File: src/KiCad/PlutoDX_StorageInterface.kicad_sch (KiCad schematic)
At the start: 14 parts, among them J2 Micro_SD_Card_Det_Hirose_DM3AT

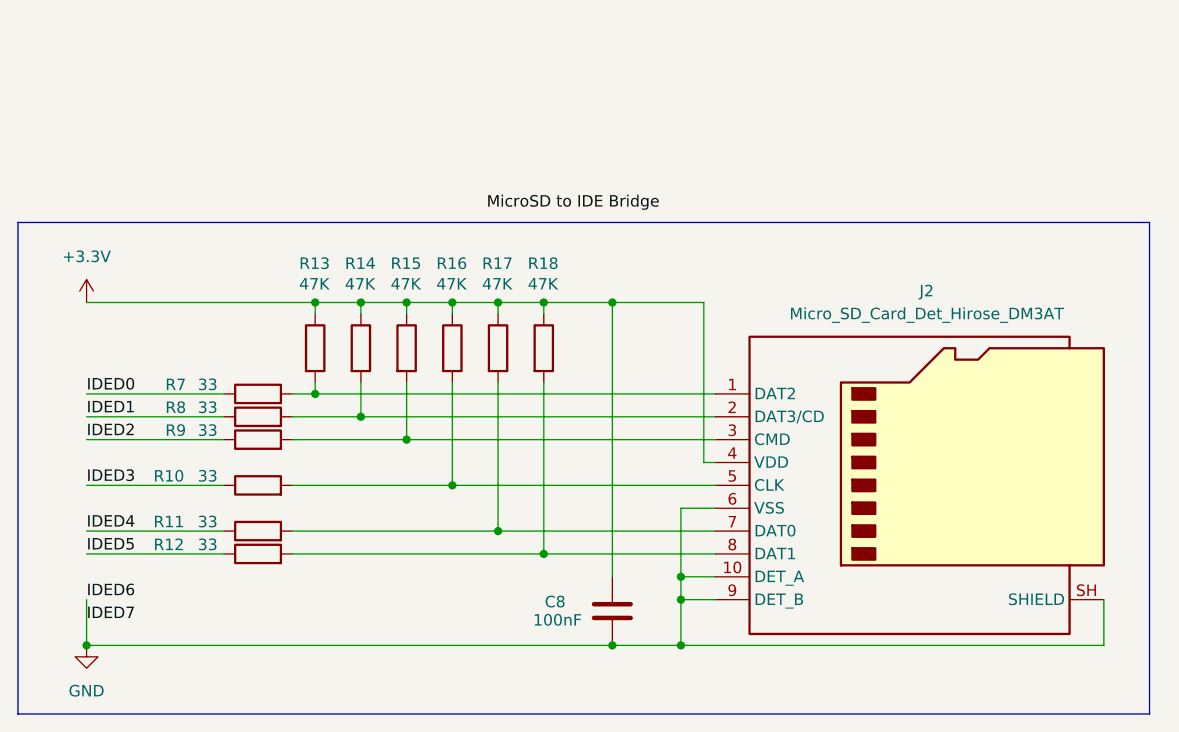
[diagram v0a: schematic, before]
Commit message: Switch to SOM304RD-PI fro mSOM304RD-VI
The SOM304RD-PI exposes a PCI bus, so PCI cards can be added. Video will now be handled via a PCI video card and/or 3D accelerator vs the SOM304RD-VI's built-in VGA video output
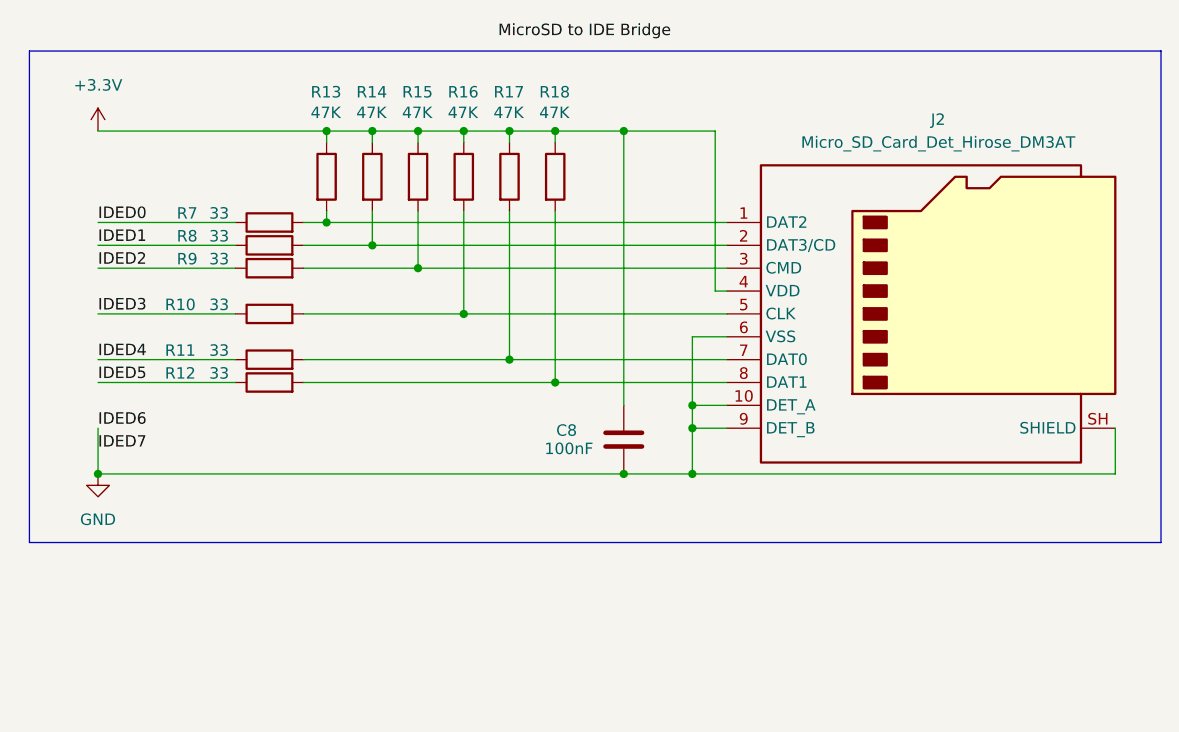
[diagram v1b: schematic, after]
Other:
- title: MicroSD to IDE Interface -> Storage Interface
- moved on the sheet: C8, J2, R10, R11, R12, R13, R14, R15, R16, R17, R18, R7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

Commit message: Add IDE connector to storage interface
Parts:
- added J3: IDE | Conn_02x20_Odd_Even, Connector_IDC:IDC-Header_2x20_P2.54mm_Vertical, symbol Connector_Generic:Conn_02x20_Odd_Even
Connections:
- net GND: now also J3.19 (Pin_19), J3.2 (Pin_2), J3.22 (Pin_22), J3.24 (Pin_24), J3.26 (Pin_26), J3.28 (Pin_28), J3.3 (Pin_3), J3.30 (Pin_30), J3.40 (Pin_40), J3.5 (Pin_5)
- net IDED0: now also J3.17 (Pin_17)
- net IDED1: now also J3.15 (Pin_15)
- net IDED2: now also J3.13 (Pin_13)
- net IDED3: now also J3.11 (Pin_11)
- net IDED4: now also J3.9 (Pin_9)
- net IDED5: now also J3.7 (Pin_7)
- new net +5V: J3.20 (Pin_20)
- new net IDEACK: J3.29 (Pin_29)
- new net IDECBLID: J3.34 (Pin_34)
- new net IDECS0: J3.37 (Pin_37)
- new net IDECS1: J3.38 (Pin_38)
- new net IDED10: J3.8 (Pin_8)
- new net IDED11: J3.10 (Pin_10)
- new net IDED12: J3.12 (Pin_12)
- new net IDED13: J3.14 (Pin_14)
- new net IDED14: J3.16 (Pin_16)
- new net IDED15: J3.18 (Pin_18)
- new net IDED8: J3.4 (Pin_4)
- new net IDED9: J3.6 (Pin_6)
- new net IDEINT: J3.31 (Pin_31)
- new net IDEIOR: J3.25 (Pin_25)
- new net IDEIOW: J3.23 (Pin_23)
- new net IDELED: J3.39 (Pin_39)
- new net IDERDY: J3.27 (Pin_27)
- new net IDEREQ: J3.21 (Pin_21)
- new net IDERST: J3.1 (Pin_1)
- new net IDESA0: J3.35 (Pin_35)
- new net IDESA1: J3.33 (Pin_33)
- new net IDESA2: J3.36 (Pin_36)
- new net NC: J3.32 (Pin_32)
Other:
- note added: "IDE Connector"
- note added: "MUST NOT BE USED WHEN IDE CONNECTOR IS USED"
- note added: "MUST NOT BE USED WHEN MicroSD CARD IS INSERTED"
- moved on the sheet: C8, J2, R10, R11, R12, R13, R14, R15, R16, R17, R18, R7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
